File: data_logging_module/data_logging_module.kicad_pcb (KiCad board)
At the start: 4 copper layers, 80 x 40 mm, 60 parts, among them J1 Conn_01x15, J2 Conn_01x15, J200 10067847-001RLF, U100 TLV62569DBV, U101 HT7533-1, U300 BME280, U301 BME280, U400 PCF8563TS, U5 DS18B20, Y400 32768Hz

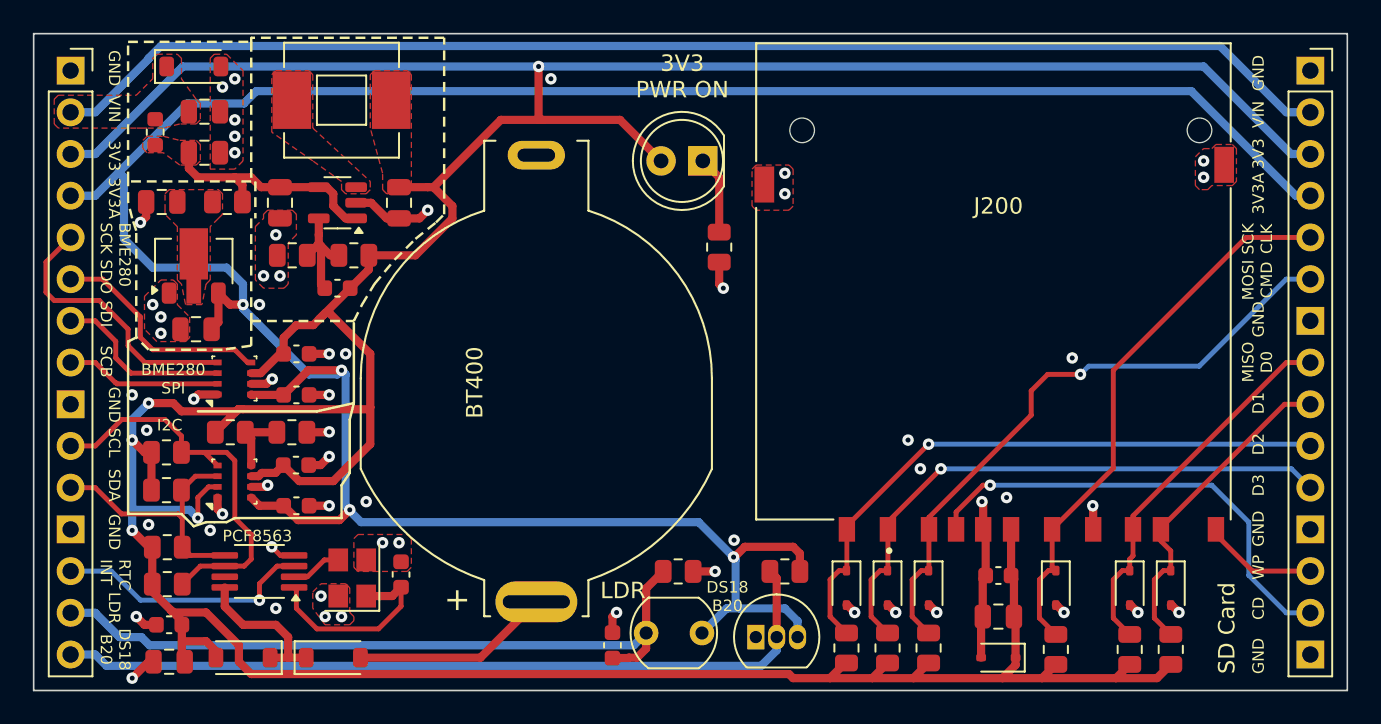
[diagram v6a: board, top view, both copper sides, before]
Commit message: Fill front and back copper layers by ground
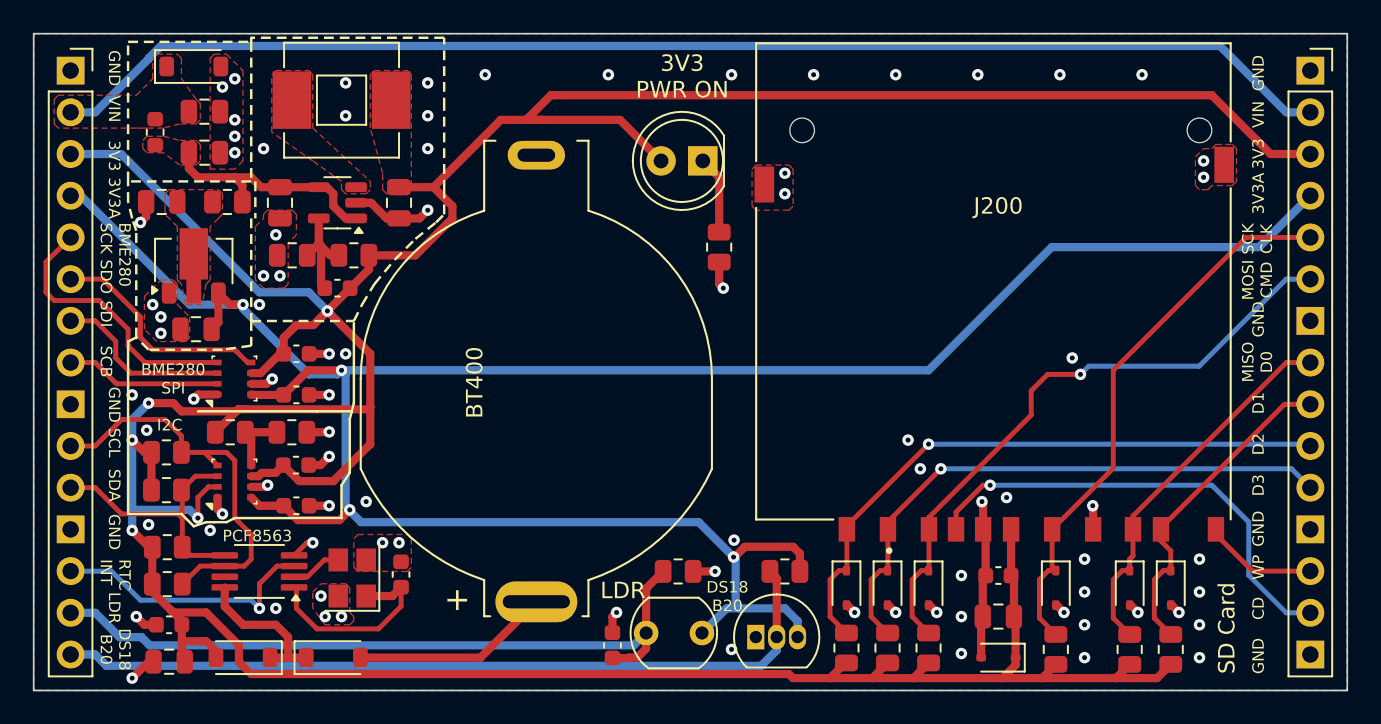
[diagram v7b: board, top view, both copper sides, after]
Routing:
- net +3.3VA: track 169.8 -> 151.9 mm
- net +3.3V: track 266.6 -> 253.6 mm
- net PCF8563_INT: track 15.8 -> 16.5 mm
- net GND: track 42.6 -> 42.5 mm, vias 59 -> 84
- added copper zone on B.Cu, net GND

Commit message: Updates in power wiring
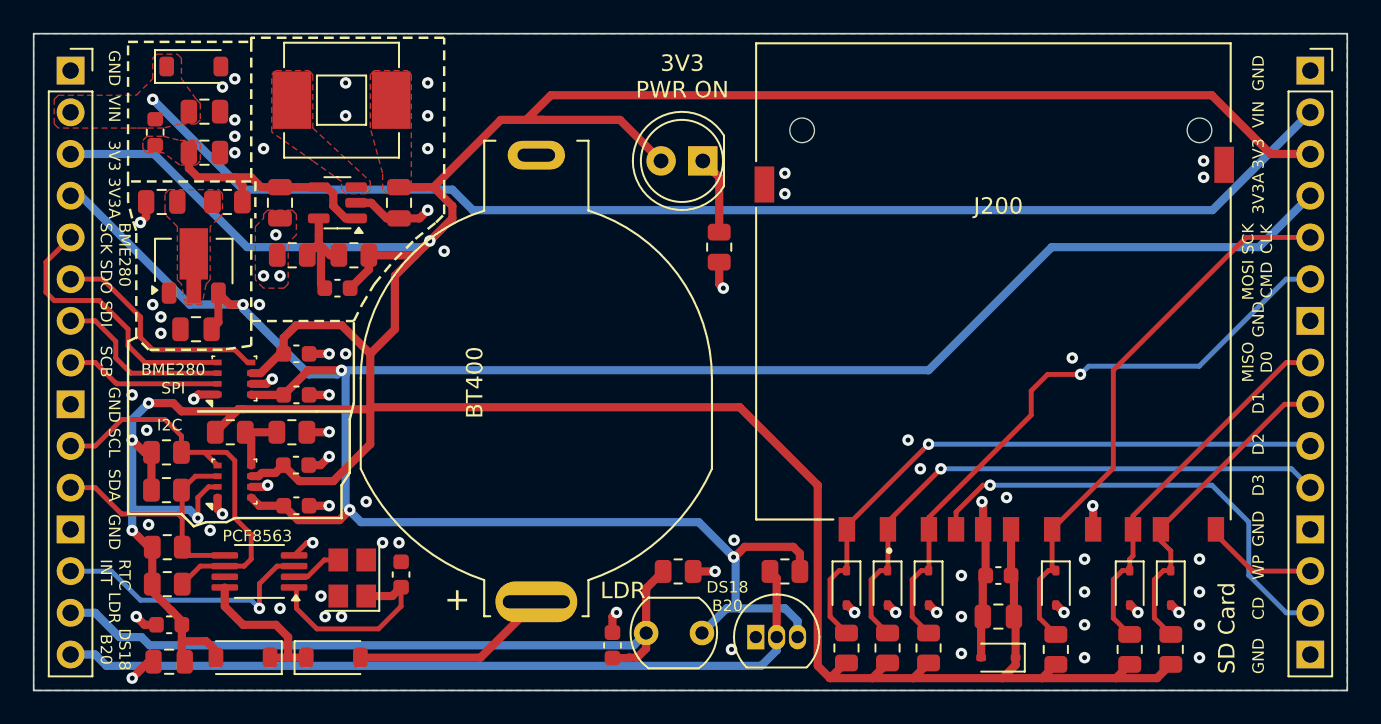
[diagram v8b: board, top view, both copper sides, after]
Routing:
- net +3.3V: track 253.6 -> 261.3 mm
- net VIN: track 78.9 -> 75.8 mm, vias 0 -> 1
- net GND: vias 84 -> 77
